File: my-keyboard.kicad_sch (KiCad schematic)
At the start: 185 parts, among them J1 AVR-ISP-6, SW1 SW_Push, U1 ATmega32U4-AU, Y1 16MHz

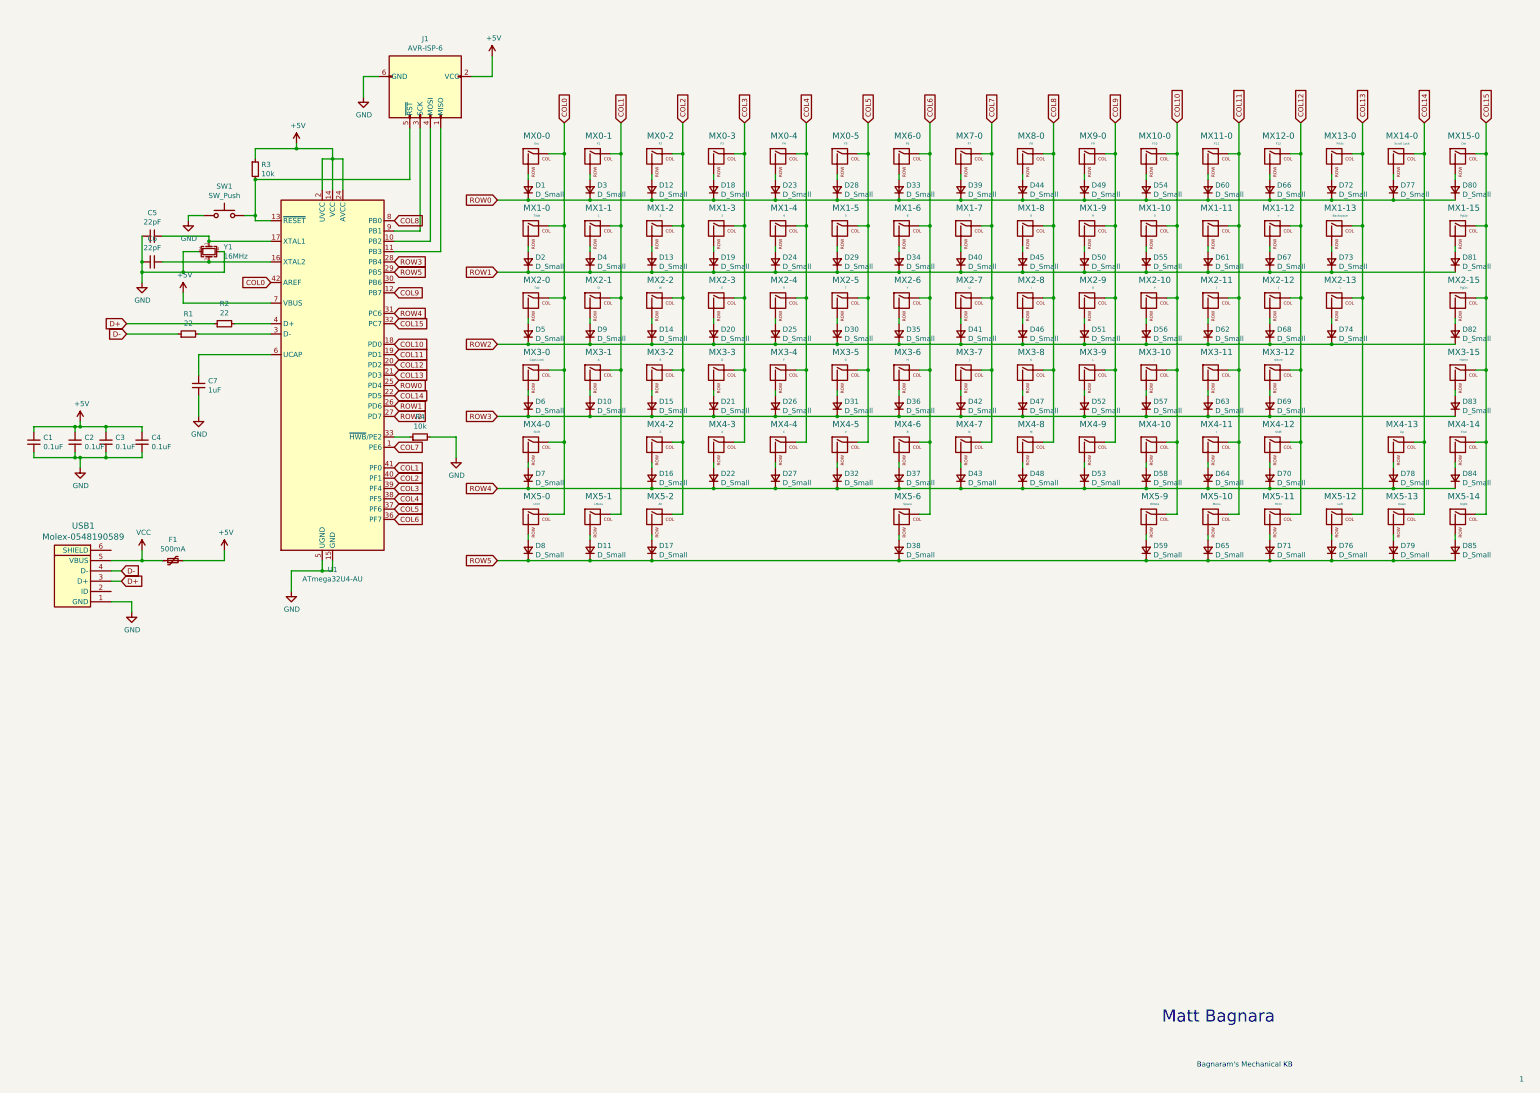
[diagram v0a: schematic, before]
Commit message: Redesign keyboard with %75 keys
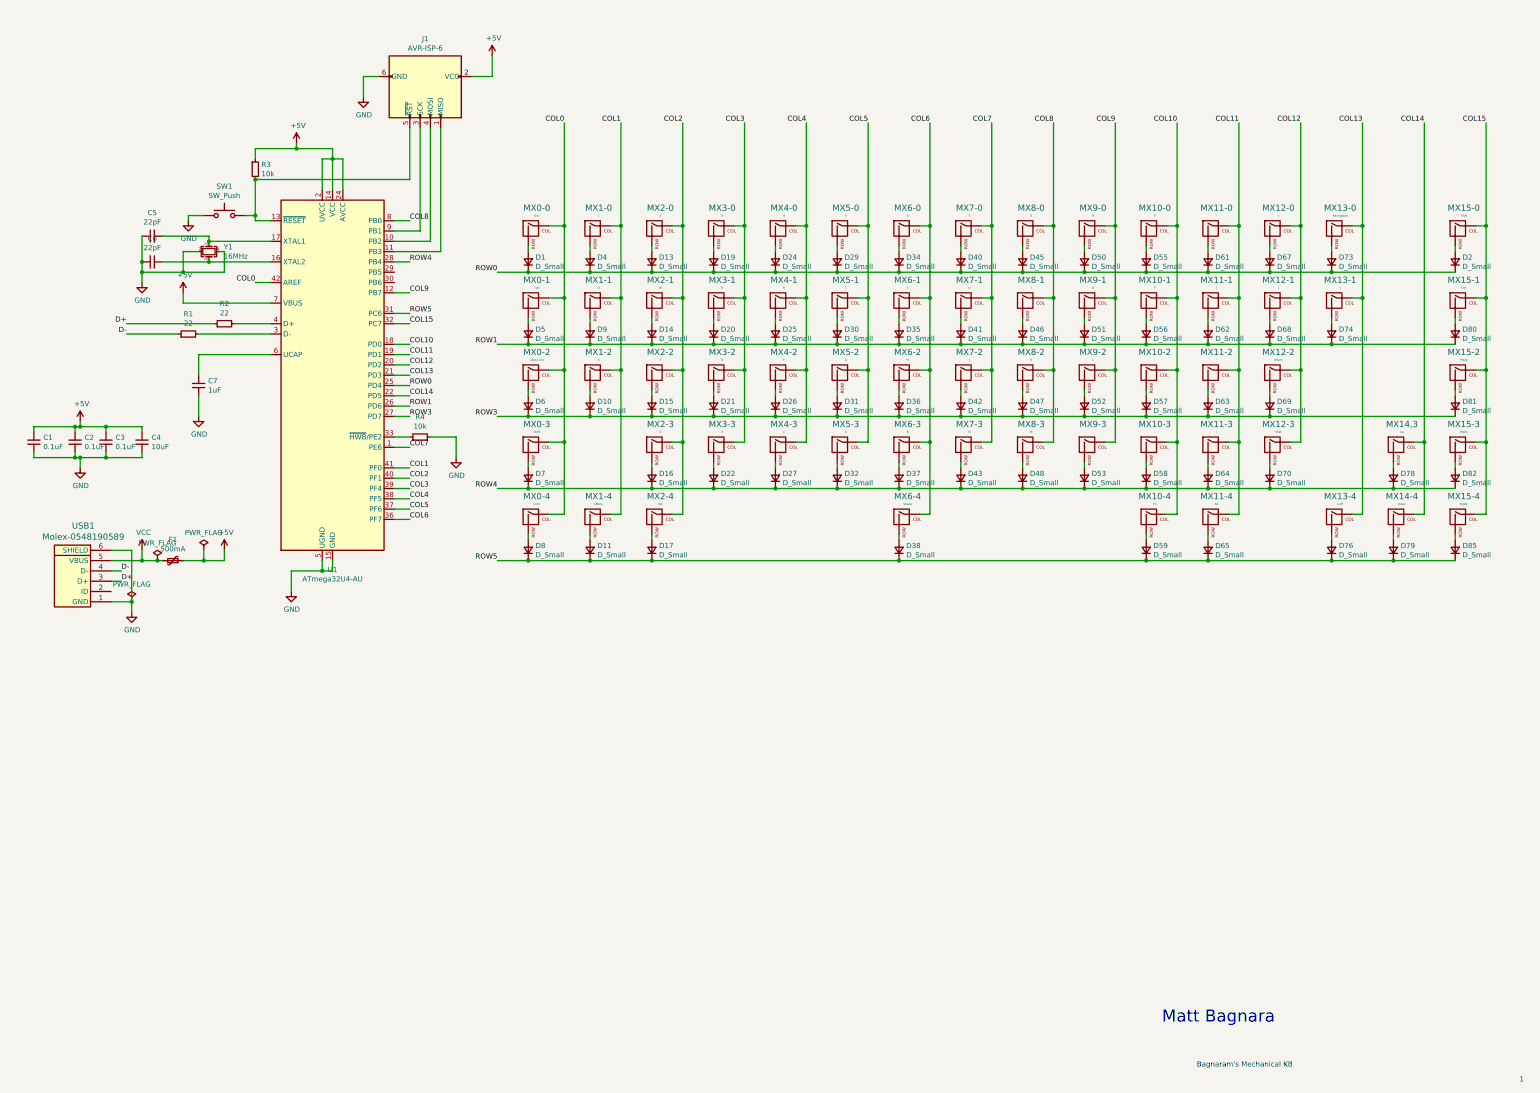
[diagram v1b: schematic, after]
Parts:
- removed D12, D18, D23, D28, D3, D33, D39, D44, D49, D54, D60, D66, D71, D72, D77, D83, D84: D_Small, Diode_SMD:D_SOD-123, symbol Device:D_Small
- removed MX0-1: F1, MX_Alps_Hybrid:MX-1U-NoLED, symbol MX_Alps_Hybrid:MX-NoLED
- removed MX0-2: F2, MX_Alps_Hybrid:MX-1U-NoLED, symbol MX_Alps_Hybrid:MX-NoLED
- removed MX0-3: F3, MX_Alps_Hybrid:MX-1U-NoLED, symbol MX_Alps_Hybrid:MX-NoLED
- removed MX0-4: F4, MX_Alps_Hybrid:MX-1U-NoLED, symbol MX_Alps_Hybrid:MX-NoLED
- removed MX0-5: F5, MX_Alps_Hybrid:MX-1U-NoLED, symbol MX_Alps_Hybrid:MX-NoLED
- removed MX10-0: F10, MX_Alps_Hybrid:MX-1U-NoLED, symbol MX_Alps_Hybrid:MX-NoLED
- removed MX11-0: F11, MX_Alps_Hybrid:MX-1U-NoLED, symbol MX_Alps_Hybrid:MX-NoLED
- removed MX12-0: F12, MX_Alps_Hybrid:MX-1U-NoLED, symbol MX_Alps_Hybrid:MX-NoLED
- removed MX13-0: PrtSc, MX_Alps_Hybrid:MX-1U-NoLED, symbol MX_Alps_Hybrid:MX-NoLED
- removed MX14-0: Scroll Lock, MX_Alps_Hybrid:MX-1U-NoLED, symbol MX_Alps_Hybrid:MX-NoLED
- removed MX3-15: Home, MX_Alps_Hybrid:MX-1U-NoLED, symbol MX_Alps_Hybrid:MX-NoLED
- removed MX4-14: End, MX_Alps_Hybrid:MX-1U-NoLED, symbol MX_Alps_Hybrid:MX-NoLED
- removed MX5-11: RCtrl, MX_Alps_Hybrid:MX-1U-NoLED, symbol MX_Alps_Hybrid:MX-NoLED
- removed MX6-0: F6, MX_Alps_Hybrid:MX-1U-NoLED, symbol MX_Alps_Hybrid:MX-NoLED
- removed MX7-0: F7, MX_Alps_Hybrid:MX-1U-NoLED, symbol MX_Alps_Hybrid:MX-NoLED
- removed MX8-0: F8, MX_Alps_Hybrid:MX-1U-NoLED, symbol MX_Alps_Hybrid:MX-NoLED
- removed MX9-0: F9, MX_Alps_Hybrid:MX-1U-NoLED, symbol MX_Alps_Hybrid:MX-NoLED
- C4: value 0.1uF -> 10uF
- MX10-4: renamed from MX5-9; value RMeta -> Fn
- MX11-4: renamed from MX5-10; value Menu -> Alt
- renumbered MX2-0 to MX0-1, MX3-0 to MX0-2, MX4-0 to MX0-3, MX5-0 to MX0-4, MX1-1 to MX1-0, MX2-1 to MX1-1, MX3-1 to MX1-2, MX5-1 to MX1-4, MX1-10 to MX10-0, MX2-10 to MX10-1, MX3-10 to MX10-2, MX4-10 to MX10-3, MX1-11 to MX11-0, MX2-11 to MX11-1, MX3-11 to MX11-2, MX4-11 to MX11-3, MX1-12 to MX12-0, MX2-12 to MX12-1, MX3-12 to MX12-2, MX4-12 to MX12-3, MX1-13 to MX13-0, MX2-13 to MX13-1, MX5-12 to MX13-4, MX4-13 to MX14,3, MX5-13 to MX14-4, MX1-0 to MX15-0, MX15-0 to MX15-1, MX1-15 to MX15-2, MX2-15 to MX15-3, MX5-14 to MX15-4, MX1-2 to MX2-0, MX2-2 to MX2-1, MX3-2 to MX2-2, MX4-2 to MX2-3, MX5-2 to MX2-4, MX1-3 to MX3-0, MX2-3 to MX3-1, MX3-3 to MX3-2, MX4-3 to MX3-3, MX1-4 to MX4-0, MX2-4 to MX4-1, MX3-4 to MX4-2, MX4-4 to MX4-3, MX1-5 to MX5-0, MX2-5 to MX5-1, MX3-5 to MX5-2, MX4-5 to MX5-3, MX1-6 to MX6-0, MX2-6 to MX6-1, MX3-6 to MX6-2, MX4-6 to MX6-3, MX5-6 to MX6-4, MX1-7 to MX7-0, MX2-7 to MX7-1, MX3-7 to MX7-2, MX4-7 to MX7-3, MX1-8 to MX8-0, MX2-8 to MX8-1, MX3-8 to MX8-2, MX4-8 to MX8-3, MX1-9 to MX9-0, MX2-9 to MX9-1, MX3-9 to MX9-2, MX4-9 to MX9-3
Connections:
- net COL0: no longer MX15-0.1 (COL)
- net COL15: now also MX15-0.1 (COL)
- net GND: now also USB1.6 (SHIELD)
- net ROW0: now also D13.1 (K), D19.1 (K), D2.1 (K), D24.1 (K), D29.1 (K), D34.1 (K), D4.1 (K), D40.1 (K), D45.1 (K), D50.1 (K), D55.1 (K), D61.1 (K), D67.1 (K), D73.1 (K); no longer D80.1 (K)
- net ROW1: now also D14.1 (K), D20.1 (K), D25.1 (K), D30.1 (K), D35.1 (K), D41.1 (K), D46.1 (K), D5.1 (K), D51.1 (K), D56.1 (K), D62.1 (K), D68.1 (K), D74.1 (K), D80.1 (K), D9.1 (K); no longer D13.1 (K), D19.1 (K), D2.1 (K), D24.1 (K), D29.1 (K), D34.1 (K), D4.1 (K), D40.1 (K), D45.1 (K), D50.1 (K), D55.1 (K), D61.1 (K), D67.1 (K), D73.1 (K), D81.1 (K)
- net ROW3: now also D81.1 (K), U1.27 (PD7); no longer U1.28 (PB4)
- net ROW4: now also D82.1 (K), U1.28 (PB4); no longer U1.31 (PC6)
- net ROW5: now also U1.31 (PC6); no longer U1.29 (PB5)
- removed net ROW2: D14.1 (K), D20.1 (K), D25.1 (K), D30.1 (K), D35.1 (K), D41.1 (K), D46.1 (K), D5.1 (K), D51.1 (K), D56.1 (K), D62.1 (K), D68.1 (K), D74.1 (K), D82.1 (K), D9.1 (K), U1.27 (PD7)
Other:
- moved on the sheet: D1, D2, D80, D81, D82, MX0-0, MX15-0, MX15-1, MX15-2, MX15-3

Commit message: optimizations, footprint change
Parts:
- removed USB1: Molex-0548190589, Random Keyboard Parts:Molex-0548190589, symbol random-keyboard-parts:Molex-0548190589
- added D86, D87: 3.6V, Diode_SMD:D_SOD-123, symbol Device:D_Zener_Small
- added R5, R6: 5.1k, Resistor_SMD:R_0805_2012Metric, symbol Device:R_Small
- added R7: 1.5k, Resistor_SMD:R_0805_2012Metric, symbol Device:R_Small
- added USB2: USB_C_GCT_USB4085-Type-C, cftkb:USB_C_GCT_USB4085, symbol discipline-pcb-rescue:USB_C_GCT_USB4085-Type-C
- F1: footprint Fuse:Fuse_1206_3216Metric -> cftkb:polyfuse_5.1mm
- J1: footprint Connector_PinHeader_1.00mm:PinHeader_2x03_P1.00mm_Horizontal -> cftkb:AVR_ICSP_3x2
- R1, R2: value 22 -> 75
- renumbered MX14,3 to MX14-3
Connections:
- net +5V: now also F1.1, R7.1; no longer F1.2
- net D+: now also D87.1 (K), USB2.A6 (DP1), USB2.B6 (DP2)
- net D-: now also D86.1 (K), R7.2, USB2.A7 (DN1), USB2.B7 (DN2)
- net GND: now also D86.2 (A), D87.2 (A), R5.2, R6.1, USB2.A1 (GND), USB2.A12 (GND), USB2.B1 (GND), USB2.B12 (GND), USB2.S1 (SHIELD)
- net VCC: now also F1.2, USB2.A4 (VBUS), USB2.A9 (VBUS), USB2.B4 (VBUS), USB2.B9 (VBUS); no longer F1.1
- new net: R5.1, USB2.B5 (CC2)
- new net: R6.2, USB2.A5 (CC1)
- no-connect marks 0 -> 4
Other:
- note added: "DECOUPLING"
- note added: "PROG"
- note added: "USB"

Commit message: image and fixup
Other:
- note added: "Bagnaram"
- note added: "Splendens"
- note removed: "Bagnaram's Mechanical KB"
- note removed: "Matt Bagnara"
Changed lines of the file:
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@@
   (junction (at 383.54 105.41) (diameter 1.016) (color 0 0 0 0))
   (junction (at 383.54 123.19) (diameter 1.016) (color 0 0 0 0))
+  (no_connect (at 45.72 198.12))
+  (no_connect (at 114.3 83.82))
   (no_connect (at 114.3 81.28))
   (no_connect (at 45.72 213.36))
-  (no_connect (at 45.72 198.12))
-  (no_connect (at 114.3 83.82))
   (wire (pts (xy 25.4 119.38) (xy 25.4 120.65))
     (stroke (width 0) (type solid) (color 0 0 0 0))
@@
     (effects (font (size 3.988 3.988)) (justify left bottom))
   )
-  (text "Matt Bagnara" (at 331.47 266.7 180)
-    (effects (font (size 2.9972 2.9972)) (justify right bottom))
-  )
-  (text "Bagnaram's Mechanical KB" (at 335.8388 277.5712 180)
+  (text "Splendens" (at 319.3641 277.5367 180)
     (effects (font (size 1.27 1.27)) (justify right bottom))
   )
+  (text "Bagnaram" (at 331.47 266.7 180)
+    (effects (font (size 2.997 2.997)) (justify right bottom))
+  )
   (text "1" (at 392.8618 281.2542 180)
